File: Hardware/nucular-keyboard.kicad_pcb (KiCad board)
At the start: 2 copper layers, 48 x 25 mm, 34 parts, among them IC1 STM32L052R6Tx, J1 JAE-AA01B-S040VA1, J2 JAE-KX14-K2D, J3 CONN_01X16, J4 CONN_01X03, Q1 IRLML6402, U1 MCP1700T-3302E/MB

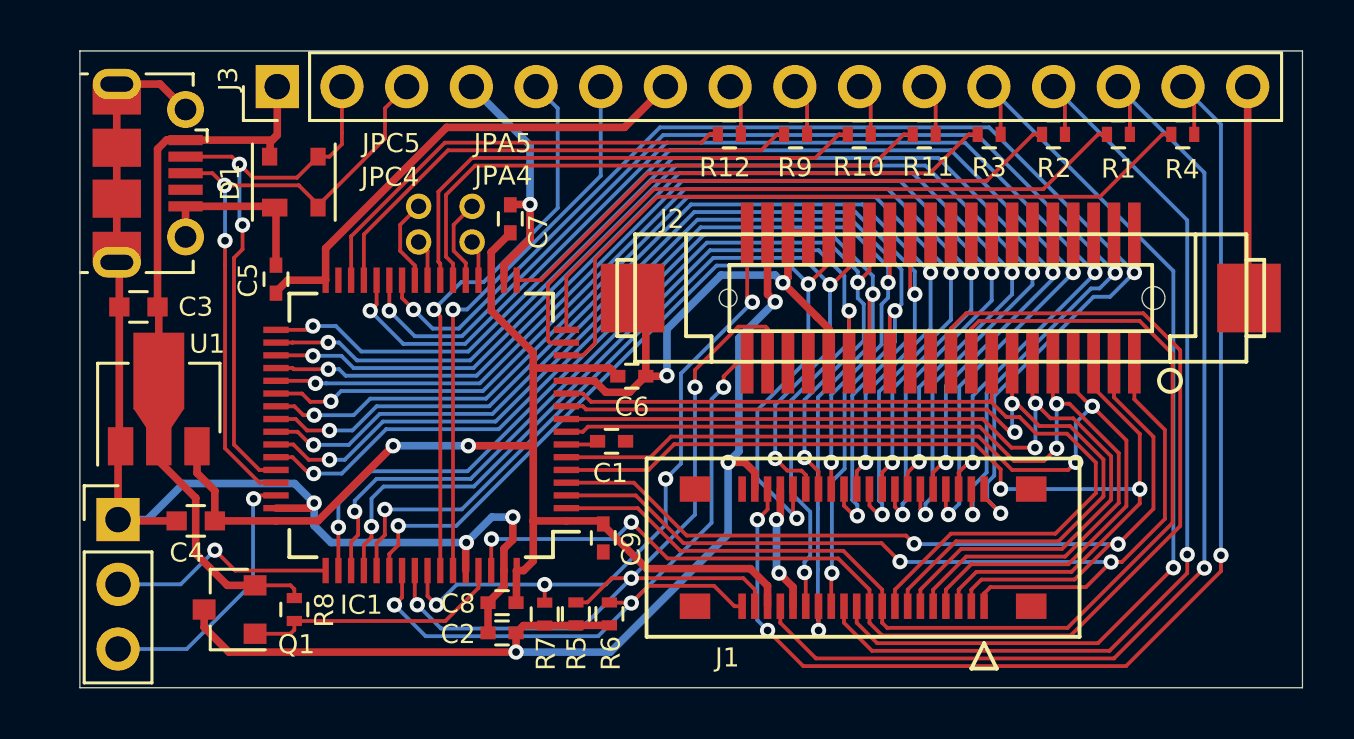
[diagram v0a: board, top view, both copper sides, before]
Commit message: Corrected footprint
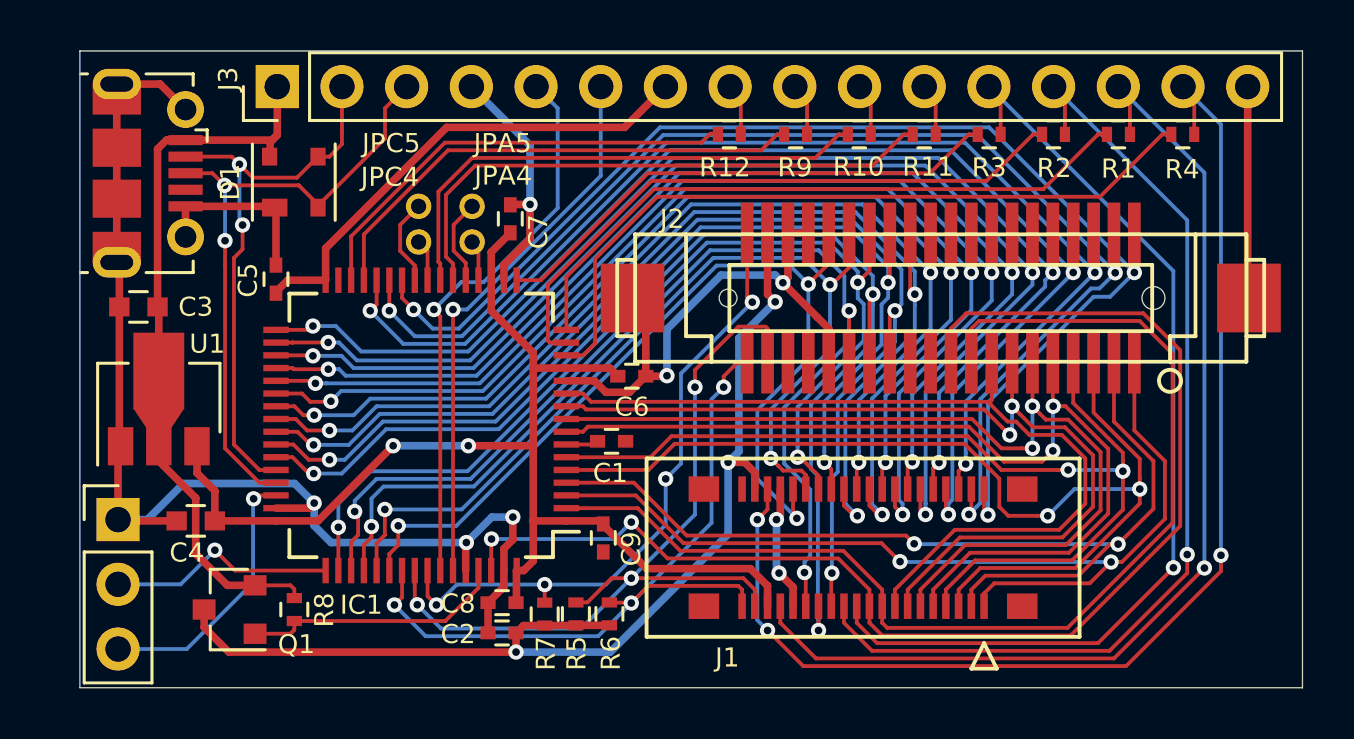
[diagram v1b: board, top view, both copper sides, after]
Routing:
- net /SENSE0: track 39.5 -> 40.6 mm
- net /SENSE3: track 39.1 -> 38.2 mm
- net /SENSE1: track 36.6 -> 36.0 mm
- net /SENSE4: track 37.4 -> 36.8 mm
- net /SENSE2: track 38.1 -> 37.5 mm

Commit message: Big clean-up
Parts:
- D1: footprint TO_SOT_Packages_SMD:SOT-143B_reflow -> _TkModules:SOT143B
- J1: value JAE-AA01B-S040VA1 -> JAE_AA01B-S040VA1; footprint Connectors_JAE:JAE_AA01B-S040VA1_2x20x0.5mm -> _TkModules:JAE_AA01B-S040VA1
- J2: value JAE-KX14-K2D -> JAE_KX14-40K2D; footprint Connectors_JAE:JAE_KX14-K2D_2x20x0.8mm -> _TkModules:JAE_KX14-40K2D
- U1: footprint TO_SOT_Packages_SMD:SOT89-3_Housing -> _TkModules:SOT89-3
- USB1: value USB_OTG -> Molex_105017-0001; footprint Connectors_USB:USB_Micro-B_Molex-105017-0001 -> _TkModules:Molex_105017-0001_USB-Micro-B

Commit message: Renamed libray to 000-xxx, so it's always on top
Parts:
- D1: footprint _TkModules:SOT143B -> 000-Modules:SOT143B
- J1: footprint _TkModules:JAE_AA01B-S040VA1 -> 000-Modules:JAE_AA01B-S040VA1
- J2: footprint _TkModules:JAE_KX14-40K2D -> 000-Modules:JAE_KX14-40K2D
- U1: footprint _TkModules:SOT89-3 -> 000-Modules:SOT89-3
- USB1: footprint _TkModules:Molex_105017-0001_USB-Micro-B -> 000-Modules:Molex_105017-0001_USB-Micro-B
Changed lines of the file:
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@@
     (add_net VCC)
   )
-  (module _TkModules:JAE_AA01B-S040VA1 (layer F.Cu)
+  (module 000-Modules:JAE_AA01B-S040VA1 (layer F.Cu)
     (at 90.75 79.5)
     (descr "40pin 0.5mm Receptable")
@@
     (pad 43 smd rect (at -6.25 2.3) (size 1.2 1) (layers F.Cu F.Paste F.Mask)
       (net 2 GND))
-    (model ${KIPRJMOD}/_TkModules.pretty/JAE_AA01B-S040VA1.wrl
+    (model ${KIPRJMOD}/000-Modules.pretty/JAE_AA01B-S040VA1.wrl
       (at (xyz 0 0 0))
       (scale (xyz 0.3937 0.3937 0.3937))
@@
     )
   )
-  (module _TkModules:JAE_KX14-40K2D (layer F.Cu)
+  (module 000-Modules:JAE_KX14-40K2D (layer F.Cu)
     (at 93.8 69.7)
     (descr "40pin 0.8mm Receptacle")
@@
     (pad "" np_thru_hole circle (at -8.35 0) (size 0.9 0.9) (drill 0.9) (layers *.Cu *.Mask))
     (pad "" np_thru_hole circle (at 8.35 0) (size 0.9 0.9) (drill 0.9) (layers *.Cu *.Mask))
-    (model ${KIPRJMOD}/_TkModules.pretty/JAE_KX14-40K2D.wrl
+    (model ${KIPRJMOD}/000-Modules.pretty/JAE_KX14-40K2D.wrl
       (at (xyz 0 0 0))
       (scale (xyz 0.3937 0.3937 0.3937))
@@
     )
   )
-  (module _TkModules:SOT143B (layer F.Cu)
+  (module 000-Modules:SOT143B (layer F.Cu)
     (at 68.4 65.15 90)
     (descr SOT143B)
@@
     )
   )
-  (module _TkModules:Molex_105017-0001_USB-Micro-B (layer F.Cu)
+  (module 000-Modules:Molex_105017-0001_USB-Micro-B (layer F.Cu)
     (at 61.8 64.8 270)
     (descr http://www.molex.com/pdm_docs/sd/1050170001_sd.pdf)
@@
     (pad 6 smd rect (at 1 0.35 270) (size 1.5 1.9) (layers F.Cu F.Paste F.Mask)
       (net 2 GND))
-    (model ${KIPRJMOD}/_TkModules.pretty/Molex_105017-0001_USB-Micro-B.wrl
+    (model ${KIPRJMOD}/000-Modules.pretty/Molex_105017-0001_USB-Micro-B.wrl
       (at (xyz 0 -0.005905511811023622 0.04921259842519685))
       (scale (xyz 0.3937 0.3937 0.3937))
@@
     )
   )
-  (module _TkModules:SOT89-3 (layer F.Cu)
+  (module 000-Modules:SOT89-3 (layer F.Cu)
     (at 63.1 74.04 90)
     (descr "SOT89-3, Housing,")
@@
       (rotate (xyz 0 0 90))
     )
-    (model ${KIPRJMOD}/_TkModules.pretty/SOT89-3.wrl
+    (model ${KIPRJMOD}/000-Modules.pretty/SOT89-3.wrl
       (at (xyz 0.01968503937007874 0 0))
       (scale (xyz 0.3937 0.3937 0.3937))

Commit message: fill polys
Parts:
- moved C3 1.50 mm to (63.8, 70.1), turned to 0 degrees
- moved C7 0.99 mm to (77.3, 67.5), turned to 0 degrees
- moved C4 0.55 mm to (64.6, 77.9), turned to 270 degrees
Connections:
- J4 pad 1: GND -> /SWDIO
- J4 pad 2: /SWCLK -> GND
- J4 pad 3: /SWDIO -> /SWCLK
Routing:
- net GND: track 100.0 -> 44.6 mm, vias 8 -> 20
- net /TP4_RESET: track 25.5 -> 29.7 mm
- net VCC: track 67.1 -> 71.1 mm, vias 2 -> 4
- net /SWDIO: track 10.6 -> 6.66 mm
- net /SWCLK: track 9.42 -> 10.8 mm
- net /KBD_ID0: track 46.2 -> 47.2 mm
- net /+5V_TP: track 42.7 -> 43.8 mm
- net /VBUS: track 29.1 -> 29.8 mm
- net /DRV13: track 36.7 -> 37.4 mm
- net /SDA/RXD: track 21.7 -> 22.3 mm
- added copper zone on B.Cu, net GND
- added copper zone on F.Cu, net GND

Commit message: plane layers
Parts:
- R1, R10, R11, R12, R2, R3, R4, R9: footprint Resistors_SMD:R_0402 -> Resistors_SMD:R_0402_NoSilk
- moved C5 0.66 mm to (67.7, 68.3), turned to 270 degrees
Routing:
- net VCC: track 71.1 -> 78.1 mm
- net GND: track 44.6 -> 47.8 mm, vias 20 -> 22
- net /LED_CAPS_R: track 38.7 -> 41.5 mm
- net /LED_POWER_R: track 39.2 -> 40.6 mm
- net /TP4_CLK: track 29.2 -> 30.1 mm
- net /KBD_ID0: track 47.2 -> 46.4 mm
- net /LED_MIC_R: track 47.6 -> 48.2 mm
- net /TP4_DATA: track 33.4 -> 34.0 mm
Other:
- board text added: "AUX"
- board text added: "CAPS"
- board text added: "LIGHT"
- board text added: "MIC"
- board text added: "MUTE"
- board text added: "NUM"
- board text added: "PWR"
- board text added: "SCRL"

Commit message: finish?
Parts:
- moved C5 1.52 mm to (69.2, 67.8), turned to 180 degrees
- moved JPA4 1.40 mm to (75.3, 66.1)
- moved JPA5 1.40 mm to (75.3, 67.5)
- moved C6 0.90 mm to (80.9, 72.3)
- moved C4 0.50 mm to (64.6, 78.4)
- moved C7 0.35 mm to (77.3, 67.2)
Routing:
- net GND: track 47.8 -> 69.6 mm, vias 22 -> 31
- net /DRV11: track 45.5 -> 43.5 mm
- net Net-(IC1-Pad21): track 3.40 -> 1.56 mm
- net Net-(IC1-Pad20): track 1.60 -> 3.36 mm
- net /TP4_RESET: track 30.0 -> 31.6 mm
- net /TP4_CLK: track 30.1 -> 31.5 mm
- net /DRV13: track 37.1 -> 35.7 mm
- net /DRV15: track 36.7 -> 35.5 mm
- net /LED_CAPS_R: track 41.5 -> 42.7 mm
- net /DRV12: track 39.1 -> 38.0 mm
- net /SENSE6: track 34.2 -> 35.2 mm
- net VCC: track 78.1 -> 77.1 mm
- net /SENSE0: track 40.2 -> 41.1 mm
- net /LED_POWER_R: track 40.6 -> 41.5 mm
- net /SENSE3: track 38.1 -> 39.0 mm
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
